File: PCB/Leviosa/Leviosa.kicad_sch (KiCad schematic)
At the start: 50 parts, among them J3 Conn_01x03, Q3 TIP122, Q4 TIP122, U1 LM324, U2 ATtiny13A-P, U3 TPS1H200AQDGNRQ1, U5 L7805, U6 SS495A

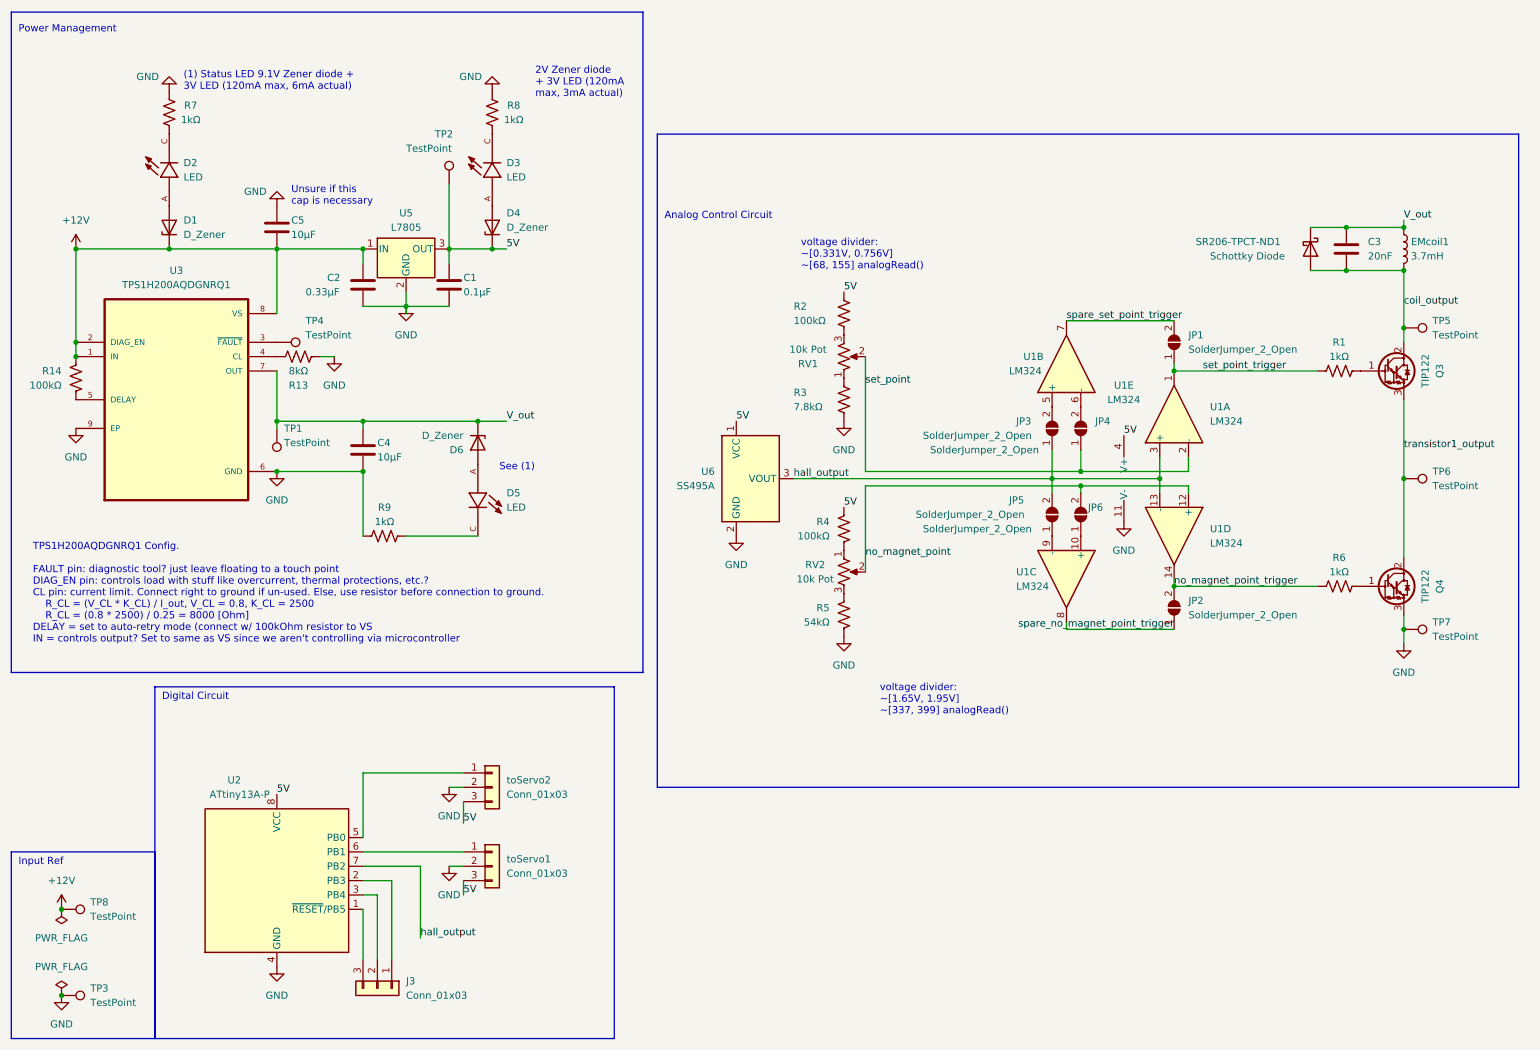
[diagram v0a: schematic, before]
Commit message: changed footprints of res and caps. changed output led to current limited.
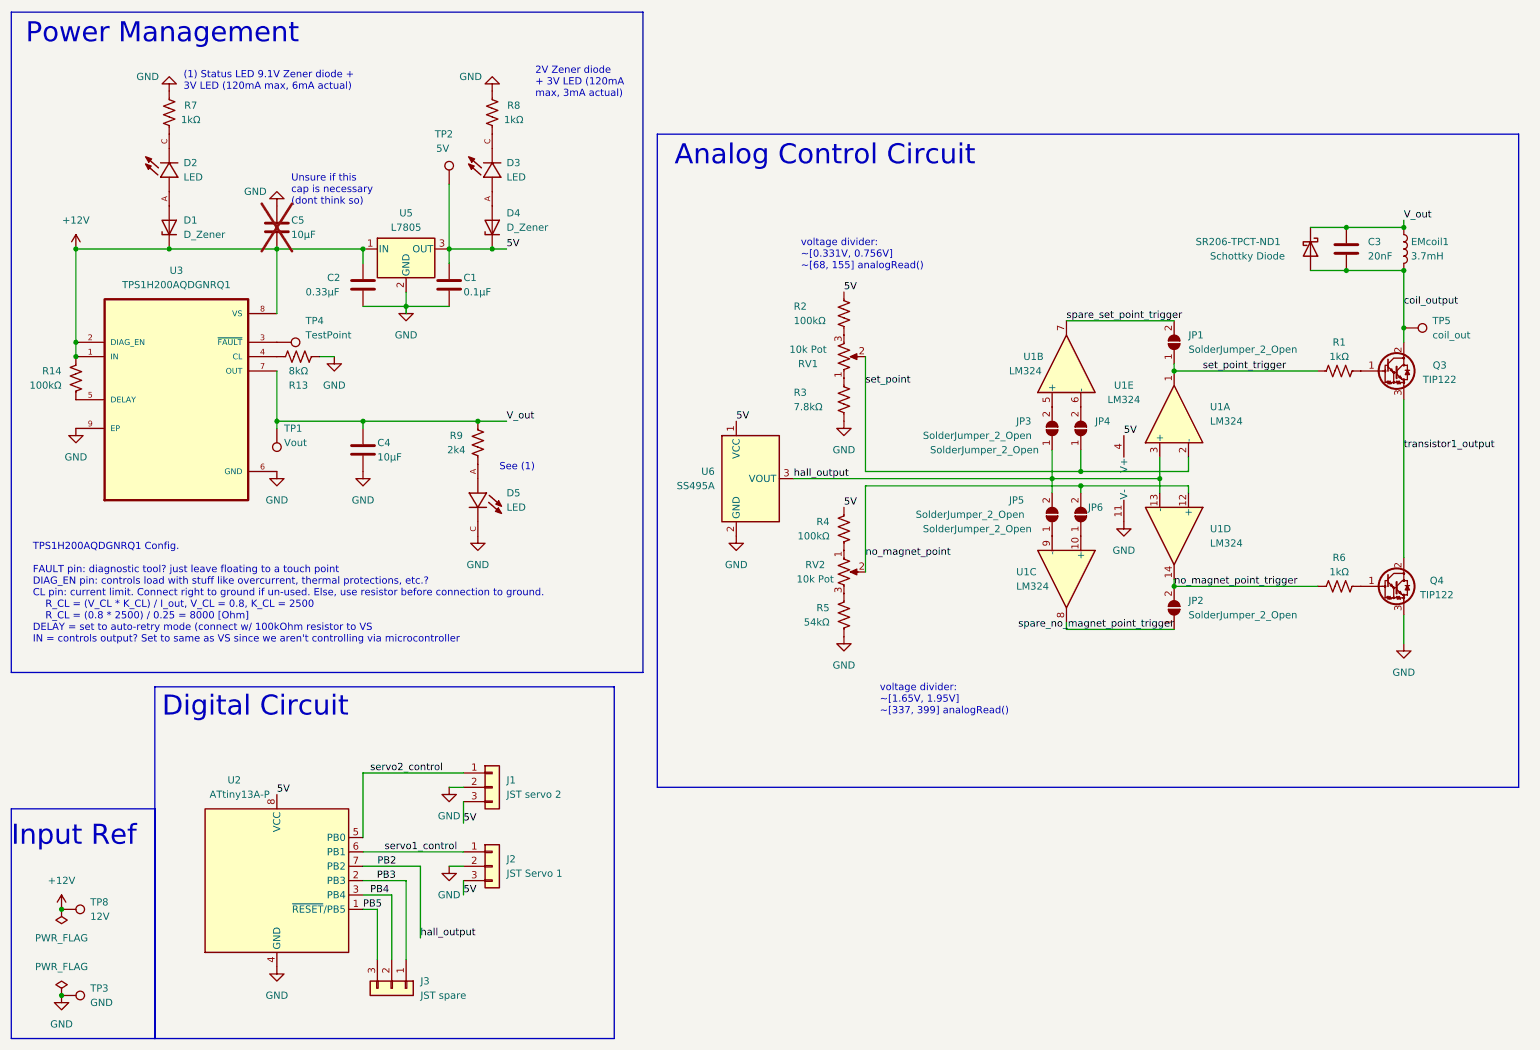
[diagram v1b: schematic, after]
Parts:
- removed D6: D_Zener, SMAZ9V1-13-F:SMA_DIO, symbol Device:D_Zener
- removed TP6, TP7: TestPoint, TestPoint:TestPoint_Pad_D3.0mm, symbol Connector:TestPoint
- C1, C2, C3, C4: footprint Capacitor_THT:CP_Axial_L10.0mm_D6.0mm_P15.00mm_Horizontal -> Capacitor_SMD:C_0805_2012Metric_Pad1.18x1.45mm_HandSolder
- C5: footprint Capacitor_THT:CP_Axial_L10.0mm_D6.0mm_P15.00mm_Horizontal -> Capacitor_SMD:C_0805_2012Metric_Pad1.18x1.45mm_HandSolder; now not fitted
- J1: renamed from toServo2; value Conn_01x03 -> JST servo 2
- J2: renamed from toServo1; value Conn_01x03 -> JST Servo 1
- J3: value Conn_01x03 -> JST spare
- R1, R13, R14, R2, R3, R4, R5, R6, R7, R8: footprint Resistor_SMD:R_0402_1005Metric_Pad0.72x0.64mm_HandSolder -> Resistor_SMD:R_0805_2012Metric_Pad1.20x1.40mm_HandSolder
- R9: value 1kΩ -> 2k4; footprint Resistor_SMD:R_0402_1005Metric_Pad0.72x0.64mm_HandSolder -> Resistor_SMD:R_0805_2012Metric_Pad1.20x1.40mm_HandSolder
- TP1: value TestPoint -> Vout
- TP2: value TestPoint -> 5V
- TP3: value TestPoint -> GND
- TP5: value TestPoint -> coil_out
- TP8: value TestPoint -> 12V
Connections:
- net GND: now also D5.C; no longer R9.2
- net V_out: now also R9.1
- net at D5.A: now also R9.2
- net PB5: now reaches J3.3 (Pin_3), U2.1 (~{RESET}/PB5)
- net PB3: now reaches J3.1 (Pin_1), U2.2 (PB3)
- net PB4: now reaches J3.2 (Pin_2), U2.3 (PB4)
- net servo2_control: now reaches J1.1 (Pin_1), U2.5 (PB0)
- net servo1_control: now reaches J2.1 (Pin_1), U2.6 (PB1)
- net hall_output renamed PB2
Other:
- note added: "Unsure if this cap is necessary (dont think so)"
- note removed: "Unsure if this cap is necessary"
- moved on the sheet: J3, R9

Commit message: add links to some components
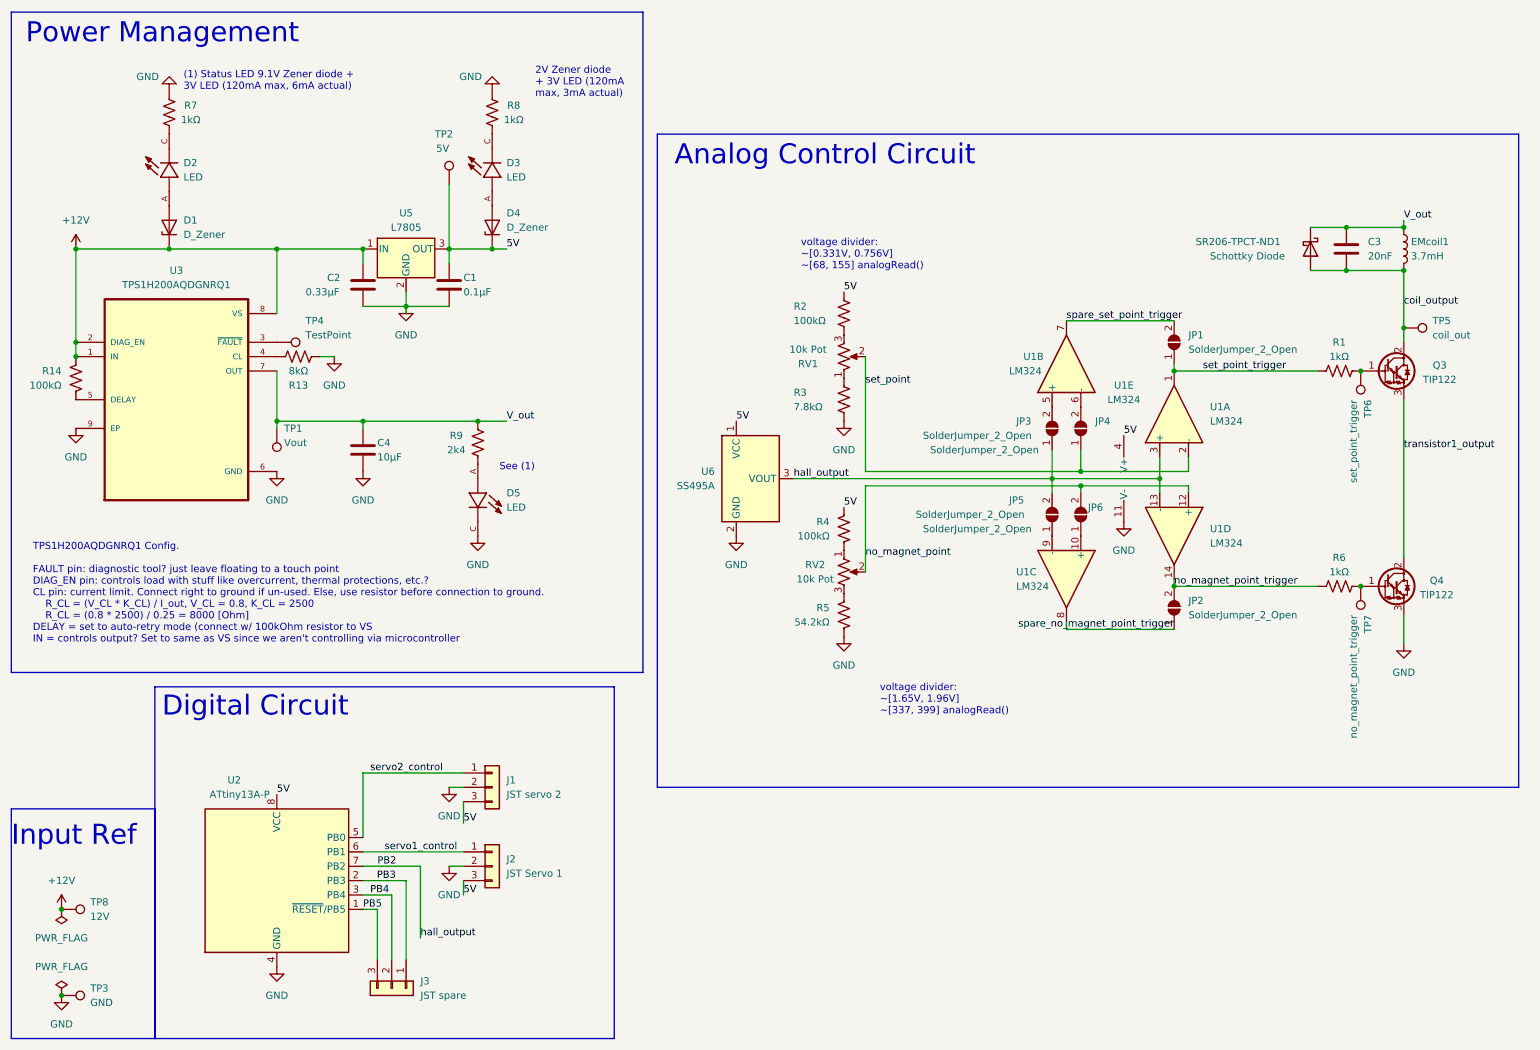
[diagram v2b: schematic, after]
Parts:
- removed C5: 10µF, Capacitor_SMD:C_0805_2012Metric_Pad1.18x1.45mm_HandSolder, symbol Device:C
- added TP6: set_point_trigger, TestPoint:TestPoint_Pad_D3.0mm, symbol Connector:TestPoint
- added TP7: no_magnet_point_trigger, TestPoint:TestPoint_Pad_D3.0mm, symbol Connector:TestPoint
- C1: Link (none) -> https://jlcpcb.com/partdetail/1943-CL10B104KB8NNNC/C1591
- C2: Link (none) -> https://jlcpcb.com/partdetail/74255-CL21B334KBFNNNE/C73142
- C3: Link (none) -> https://jlcpcb.com/partdetail/1954-0603B203K500NT/C1602
- Q3, Q4: Link (none) -> https://jlcpcb.com/partdetail/STMicroelectronics-TIP122/C16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
- R14, R2, R4: Link (none) -> https://jlcpcb.com/partdetail/738376-RCT06100KFLF/C702843
- R5: value 54kΩ -> 54.2kΩ; Link (none) -> https://jlcpcb.com/partdetail/YAGEO-RT0402BRD0754K2L/C852840
- U1: Link (none) -> https://jlcpcb.com/partdetail/TexasInstruments-LM324NNOPB/C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
- U3: Link (none) -> https://jlcpcb.com/partdetail/TexasInstruments-TPS1H200AQDG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
- U5: Link (none) -> https://jlcpcb.com/partdetail/STMicroelectronics-L7805CVDG/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
- U6: Link (none) -> https://jlcpcb.com/partdetail/Honeywell-SS495A/C126668
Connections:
- net at Q3.1 (B), R1.1: now also TP6.1
- net at Q4.1 (B), R6.1: now also TP7.1
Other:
- note added: "voltage divider: ~[1.65V, 1.96V] ~[337, 399] analogRead()"
- note removed: "Unsure if this cap is necessary (dont think so)"
- note removed: "voltage divider: ~[1.65V, 1.95V] ~[337, 399] analogRead()"
